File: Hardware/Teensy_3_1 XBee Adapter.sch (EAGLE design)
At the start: 34 parts

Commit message: Opened the board up a bit
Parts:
- removed EXT_PWR: M02PTH, SparkFun-Connectors:M02PTH
- added EXT_3.3V: M02PTH, SparkFun-Connectors:M02PTH
- JP1: value TEENSY-3.1 -> TEENSY-3.1NOSILK; device Testing:TEENSY-3.1 -> Testing:TEENSY-3.1NOSILK
- LOGO2: value OSHW-LOGOS -> OSHW-LOGOM; device SparkFun-Aesthetics:OSHW-LOGOS -> SparkFun-Aesthetics:OSHW-LOGOM
- LOGO3: value SFE_LOGO_NAME_FLAME.1_INCH -> SFE_LOGO_NAME_FLAME.2_INCH; device SparkFun-Aesthetics:SFE_LOGO_NAME_FLAME.1_INCH -> SparkFun-Aesthetics:SFE_LOGO_NAME_FLAME.2_INCH
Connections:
- removed net EXT_PWR: EXT_PWR.2, SJ4.1, SJ5.2
- new net EXT_3.3V: EXT_3.3V.2, SJ4.1, SJ5.2
- net GND: now also EXT_3.3V.1; no longer EXT_PWR.1
- net IN: now also S2.5; no longer S2.2
- net N$140: now also S2.6; no longer S2.3
- net N$141: now also S2.3; no longer S2.6
- net OUT: now also S2.2; no longer S2.5
- net UART_RX: now also S2.1; no longer S2.4
- net UART_TX: now also S2.4; no longer S2.1
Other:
- note added: "Bridge VIN-EXT_PWR jumper to source Teensy from EXT_PWR. Supply a regulated 3.3 volts."
- note added: "CAUTION: Do not attach USB in this mode unless the Teensy's VUSB-VIN jumper is open."
- note added: "LEDs"
- note added: "Power"
- note added: "Set XBee serial to hardware UART1 or software UART on pins 20/21. Open jumpers to isolate the digital pins."
- note added: "Switches"
- note added: "Teensy 3.1"
- note added: "The Teensy regulates 3.3v up to 100mA"
- note added: "Use to set XBee source. When using external power, supply a regulated 3.3v."
- note added: "XBee"
- moved on the sheet: LED1, LED2, LED3, LED4, LED5, R1, R11, R2, R3, R4, S3, U$2

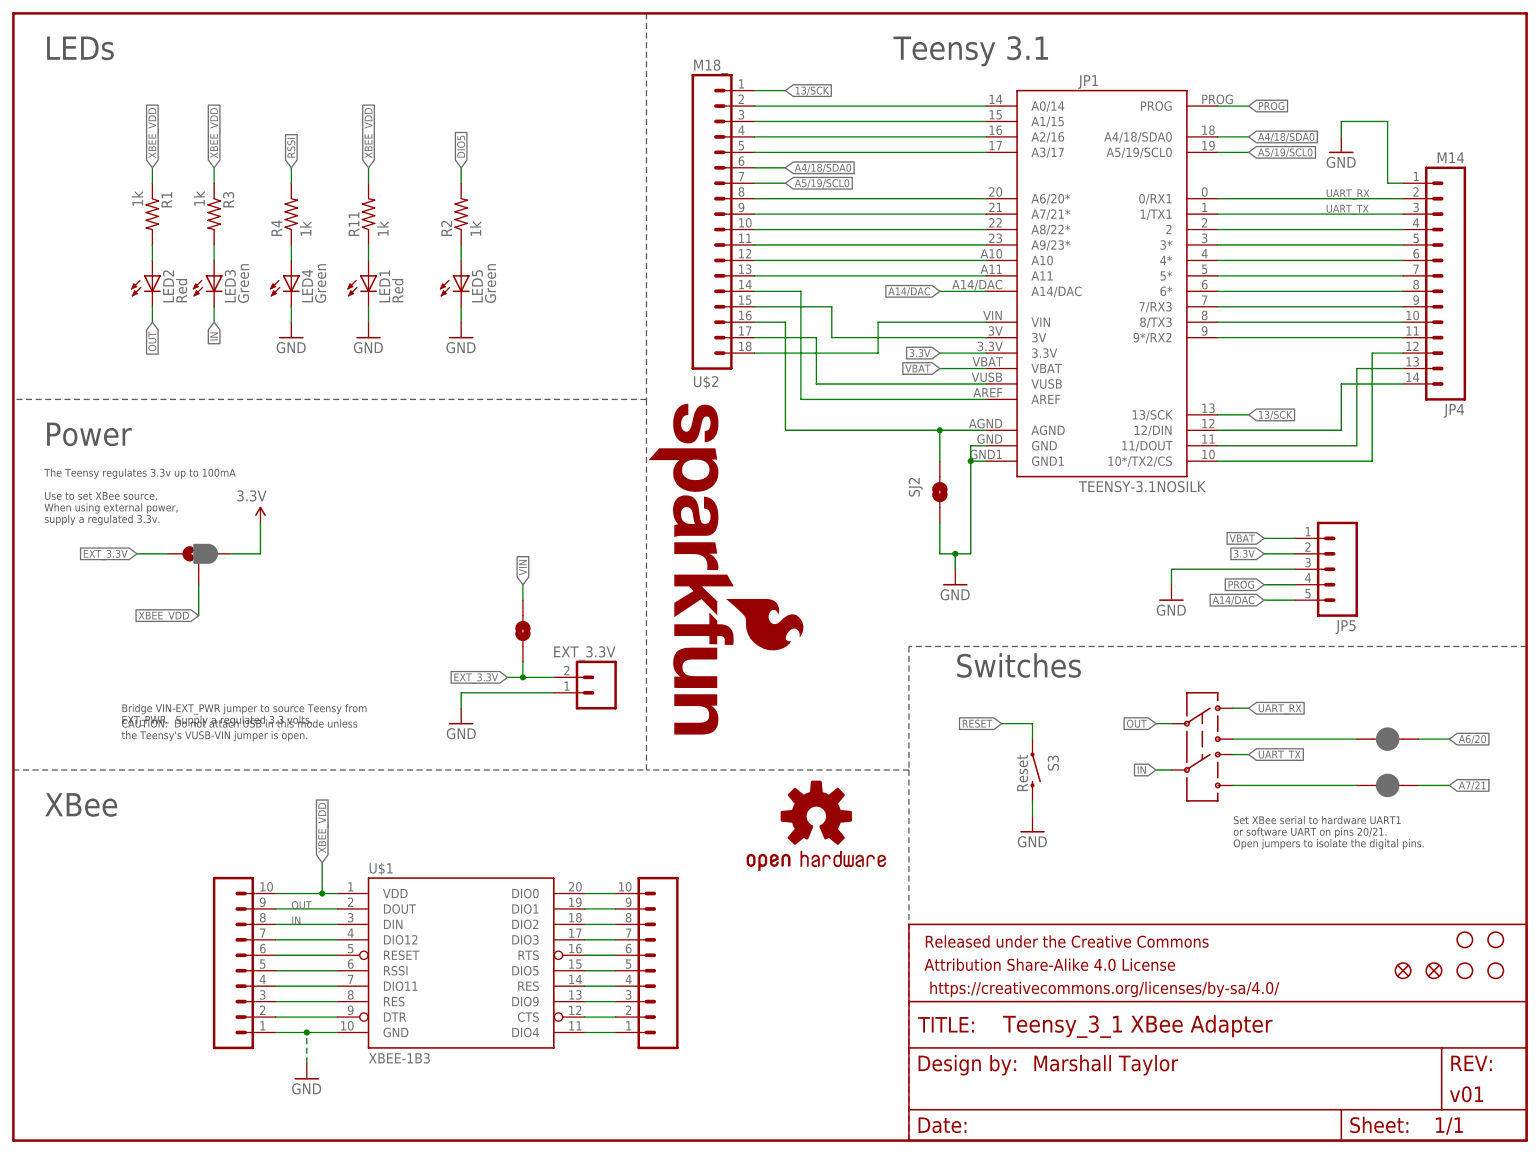
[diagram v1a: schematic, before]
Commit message: Fixed silk.  Preparing for first proto
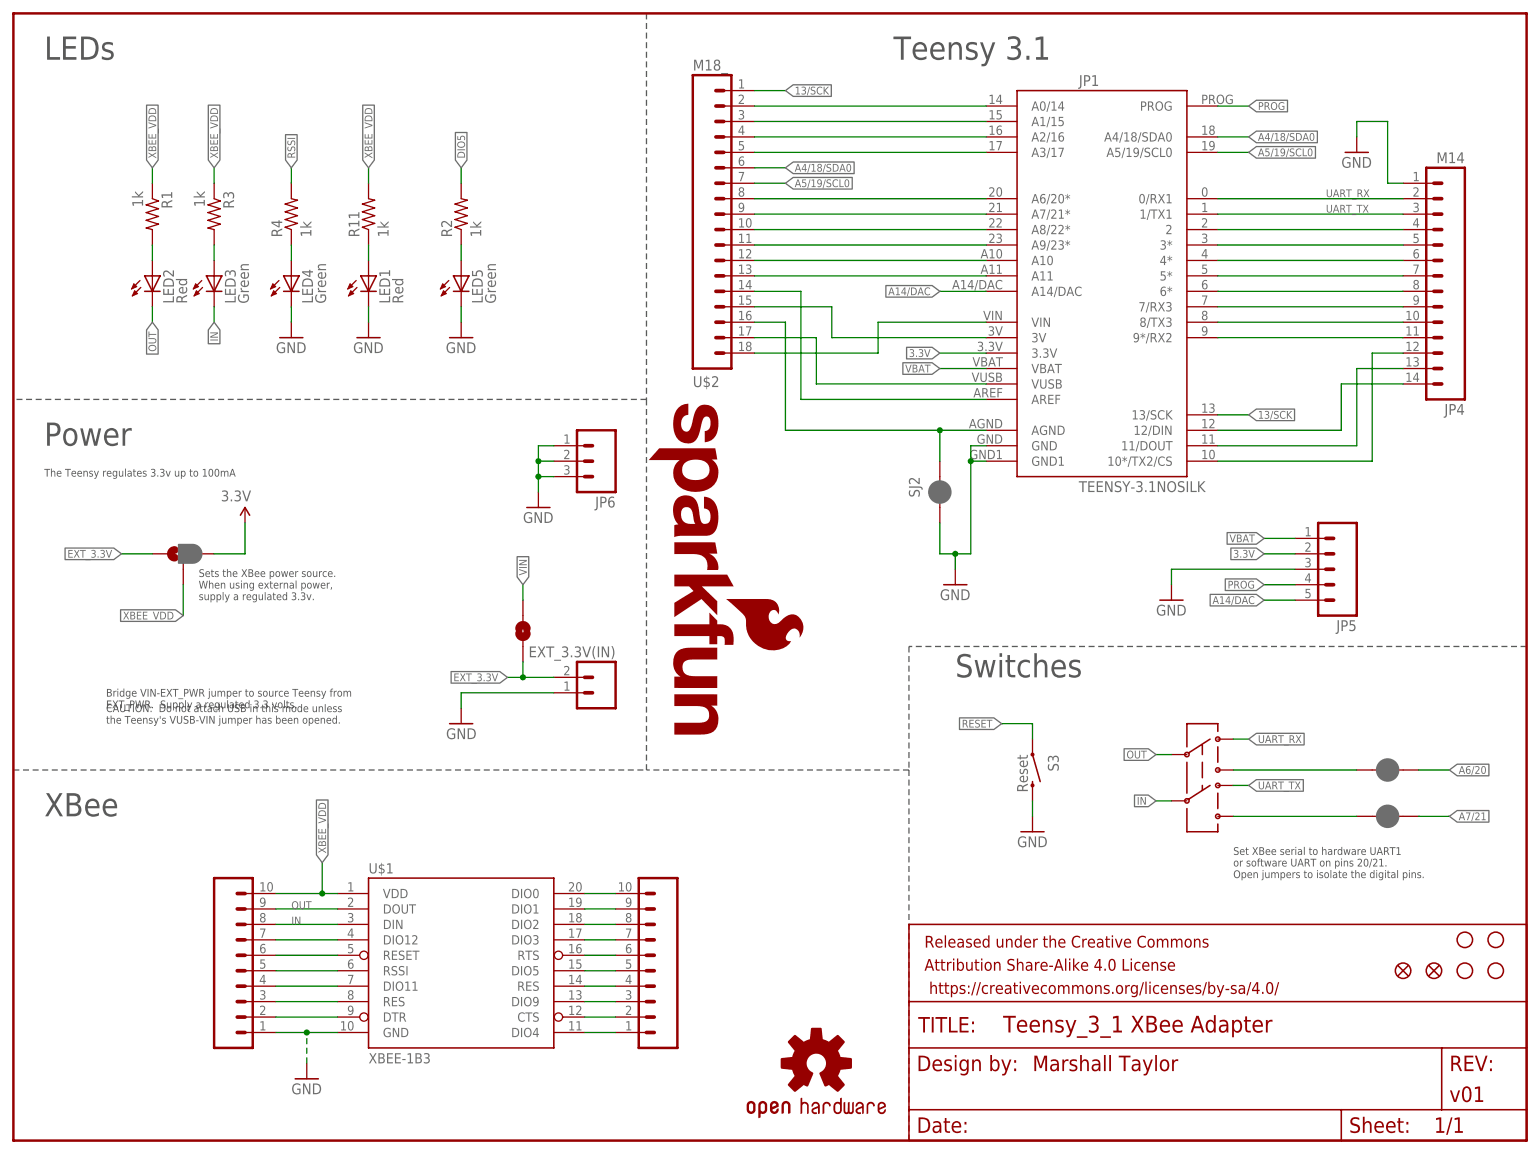
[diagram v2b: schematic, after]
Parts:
- added JP6: (no value), SparkFun-Connectors:M03PTH
- FID1, FID2: value FIDUCIAL1X2 -> FIDUCIALUFIDUCIAL; device SparkFun-Aesthetics:FIDUCIAL1X2 -> SparkFun-Aesthetics:FIDUCIALUFIDUCIAL
- SJ2: device SparkFun:SOLDERJUMPERNC -> SparkFun-Passives:JUMPER-PAD-2-NC_BY_PASTE
- renumbered EXT_3.3V to EXT_3.3V(IN)
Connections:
- net GND: now also JP6.1, JP6.2, JP6.3
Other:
- note added: "CAUTION: Do not attach USB in this mode unless the Teensy's VUSB-VIN jumper has been opened."
- note added: "Sets the XBee power source. When using external power, supply a regulated 3.3v."
- note removed: "CAUTION: Do not attach USB in this mode unless the Teensy's VUSB-VIN jumper is open."
- note removed: "Use to set XBee source. When using external power, supply a regulated 3.3v."

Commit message: Completed first round of QC notes
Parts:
- removed EXT_3.3V(IN): M02PTH, SparkFun-Connectors:M02PTH
- removed U$2: M18_, SparkFun-Connectors:M18_
- added JP7: DNP\, SparkFun-Connectors:M18_
- added JP8: DNP, SparkFun-Connectors:M02PTH
- JP2, JP3: value M10NO_SILK_PTH_FEMALE -> (none)
- JP4: value M14 -> DNP
- JP5, JP6: value (none) -> DNP
- JP9: value XBEE-1B3 -> CONN-09042
- S2: value SWITCH-DPDTSMD -> DPDT; device SparkFun:SWITCH-DPDTSMD -> SparkFun-Electromechanical:SWITCH-DPDTAYZ0202
- S3: device SparkFun:SWITCH-MOMENTARY-2SMD -> SparkFun-Electromechanical:SWITCH-MOMENTARY-2SMD
- renumbered U$1 to JP9
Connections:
- net 13/SCK: now also JP7.18; no longer U$2.1
- net 3V: now also JP7.4; no longer U$2.15
- net A0/14: now also JP7.17; no longer U$2.2
- net A1/15: now also JP7.16; no longer U$2.3
- net A10: now also JP7.7; no longer U$2.12
- net A11: now also JP7.6; no longer U$2.13
- net A2/16: now also JP7.15; no longer U$2.4
- net A3/17: now also JP7.14; no longer U$2.5
- net A4/18/SDA0: now also JP7.13; no longer U$2.6
- net A5/19/SCL0: now also JP7.12; no longer U$2.7
- net A6/20: now also JP7.11; no longer U$2.8
- net A7/21: now also JP7.10; no longer U$2.9
- net A8/22: now also JP7.9; no longer U$2.10
- net A9/23: now also JP7.8; no longer U$2.11
- net AGND: now also JP7.3; no longer U$2.16
- net AREF: now also JP7.5; no longer U$2.14
- net EXT_3.3V: now also JP8.1; no longer EXT_3.3V(IN).2
- net GND: now also JP8.2; no longer EXT_3.3V(IN).1
- net VIN: now also JP7.1; no longer U$2.18
- net VUSB: now also JP7.2; no longer U$2.17
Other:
- note added: "DPDT"
- note added: "Open to seperate AGND from GND"

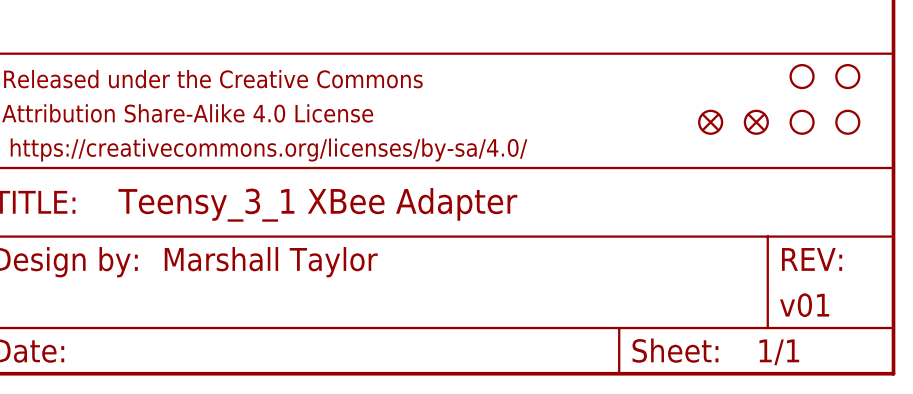
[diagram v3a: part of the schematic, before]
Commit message: Fixed airwire, updated revision
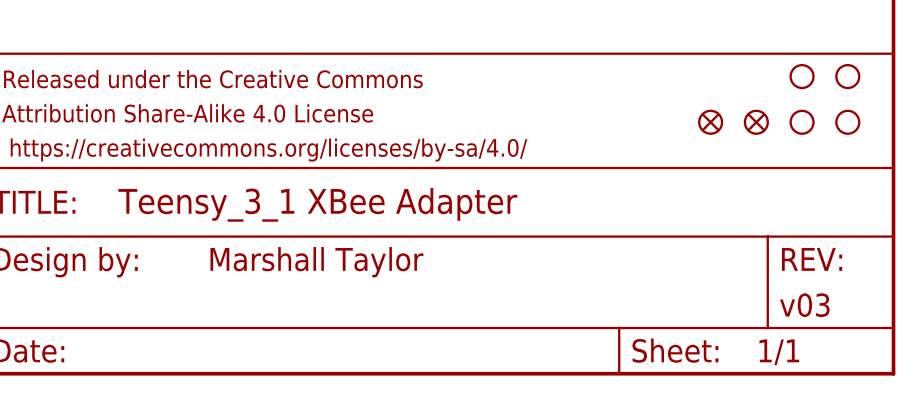
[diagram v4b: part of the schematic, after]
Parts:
- FRAME1: VERSION (none) -> v03
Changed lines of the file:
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@@
 <part name="FRAME1" library="SparkFun-Aesthetics" deviceset="FRAME-LETTER" device="">
 <attribute name="DESIGNER" value="Marshall Taylor"/>
+<attribute name="VERSION" value="v03"/>
 </part>
 <part name="JP1" library="Testing" deviceset="TEENSY-3.1" device="NOSILK"/>
@@
 <instance part="FRAME1" gate="G$1" x="0" y="0"/>
 <instance part="FRAME1" gate="V" x="147.32" y="0">
-<attribute name="DESIGNER" x="167.64" y="12.7" size="2.54" layer="94" font="vector" align="center-left"/>
+<attribute name="DESIGNER" x="172.72" y="12.7" size="2.54" layer="94" font="vector" align="center-left"/>
 <attribute name="VERSION" x="236.22" y="7.62" size="2.54" layer="94" font="vector" align="center-left"/>
 </instance>
